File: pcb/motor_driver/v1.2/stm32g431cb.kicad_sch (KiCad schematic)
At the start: 36 parts, among them J3 Conn_ARM_JTAG_SWD_10, J5 Conn, SW1 SKRPACE010, SW2 SKRPACE010, U10 STM32G431CB, U12 MCP2562-E-SN, Y1 XRCGB16M000FXN02R0

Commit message: perf: fix pcb for v1.2
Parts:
- removed SW1, SW2: SKRPACE010, bldc_lib:SKRPACE010, symbol bldc_lib:SKRPACE010
- added SW1: RESET, half_mouse_lib:TVAF06-A020B-R, symbol My_Device:SKRPACE
- added SW2: USER, half_mouse_lib:TVAF06-A020B-R, symbol My_Device:SKRPACE
- C22: renamed from C26; footprint Capacitor_SMD:C_0402_1005Metric -> Capacitor_SMD:C_0603_1608Metric
- C23: renamed from C27; footprint Capacitor_SMD:C_0201_0603Metric -> Capacitor_SMD:C_0603_1608Metric
- C24: renamed from C29; footprint Capacitor_SMD:C_0201_0603Metric -> Capacitor_SMD:C_0603_1608Metric
- C25: renamed from C30; footprint Capacitor_SMD:C_0201_0603Metric -> Capacitor_SMD:C_0603_1608Metric
- C27: renamed from C34; footprint Capacitor_SMD:C_0402_1005Metric -> Capacitor_SMD:C_0603_1608Metric
- C28: renamed from C36; footprint Capacitor_SMD:C_0201_0603Metric -> Capacitor_SMD:C_0603_1608Metric
- D2: renamed from D5; footprint LED_SMD:LED_0402_1005Metric -> LED_SMD:LED_0603_1608Metric
- D3: renamed from D6; footprint LED_SMD:LED_0402_1005Metric -> LED_SMD:LED_0603_1608Metric
- D4: renamed from D7; footprint LED_SMD:LED_0402_1005Metric -> LED_SMD:LED_0603_1608Metric
- D5: renamed from D8; footprint LED_SMD:LED_0402_1005Metric -> LED_SMD:LED_0603_1608Metric
- D6: renamed from D9; footprint LED_SMD:LED_0402_1005Metric -> LED_SMD:LED_0603_1608Metric
- D7: renamed from D10; footprint LED_SMD:LED_0402_1005Metric -> LED_SMD:LED_0603_1608Metric
- R17: renamed from R22; footprint Resistor_SMD:R_0201_0603Metric -> Resistor_SMD:R_0603_1608Metric_Pad0.98x0.95mm_HandSolder
- R18: renamed from R24; footprint Resistor_SMD:R_0201_0603Metric -> Resistor_SMD:R_0603_1608Metric_Pad0.98x0.95mm_HandSolder
- R19: renamed from R23; footprint Resistor_SMD:R_0201_0603Metric -> Resistor_SMD:R_0603_1608Metric_Pad0.98x0.95mm_HandSolder
- R20: renamed from R25; footprint Resistor_SMD:R_0201_0603Metric -> Resistor_SMD:R_0603_1608Metric_Pad0.98x0.95mm_HandSolder
- renumbered C20 to C19, C21 to C20, C25 to C21, C33 to C26, J3 to J4, R14 to R11, R15 to R12, R16 to R13, R17 to R14, R18 to R15, R19 to R16, R26 to R21, R27 to R22, R28 to R23, U10 to U5, U12 to U6
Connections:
- net +3.3V: no longer C26.1
- net GND: now also SW1.2, SW2.1
- net NRST: now also SW1.1
- net SW1: now also C26.1, R18.2, SW2.2
- no-connect marks 3 -> 2
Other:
- moved on the sheet: C21, R18

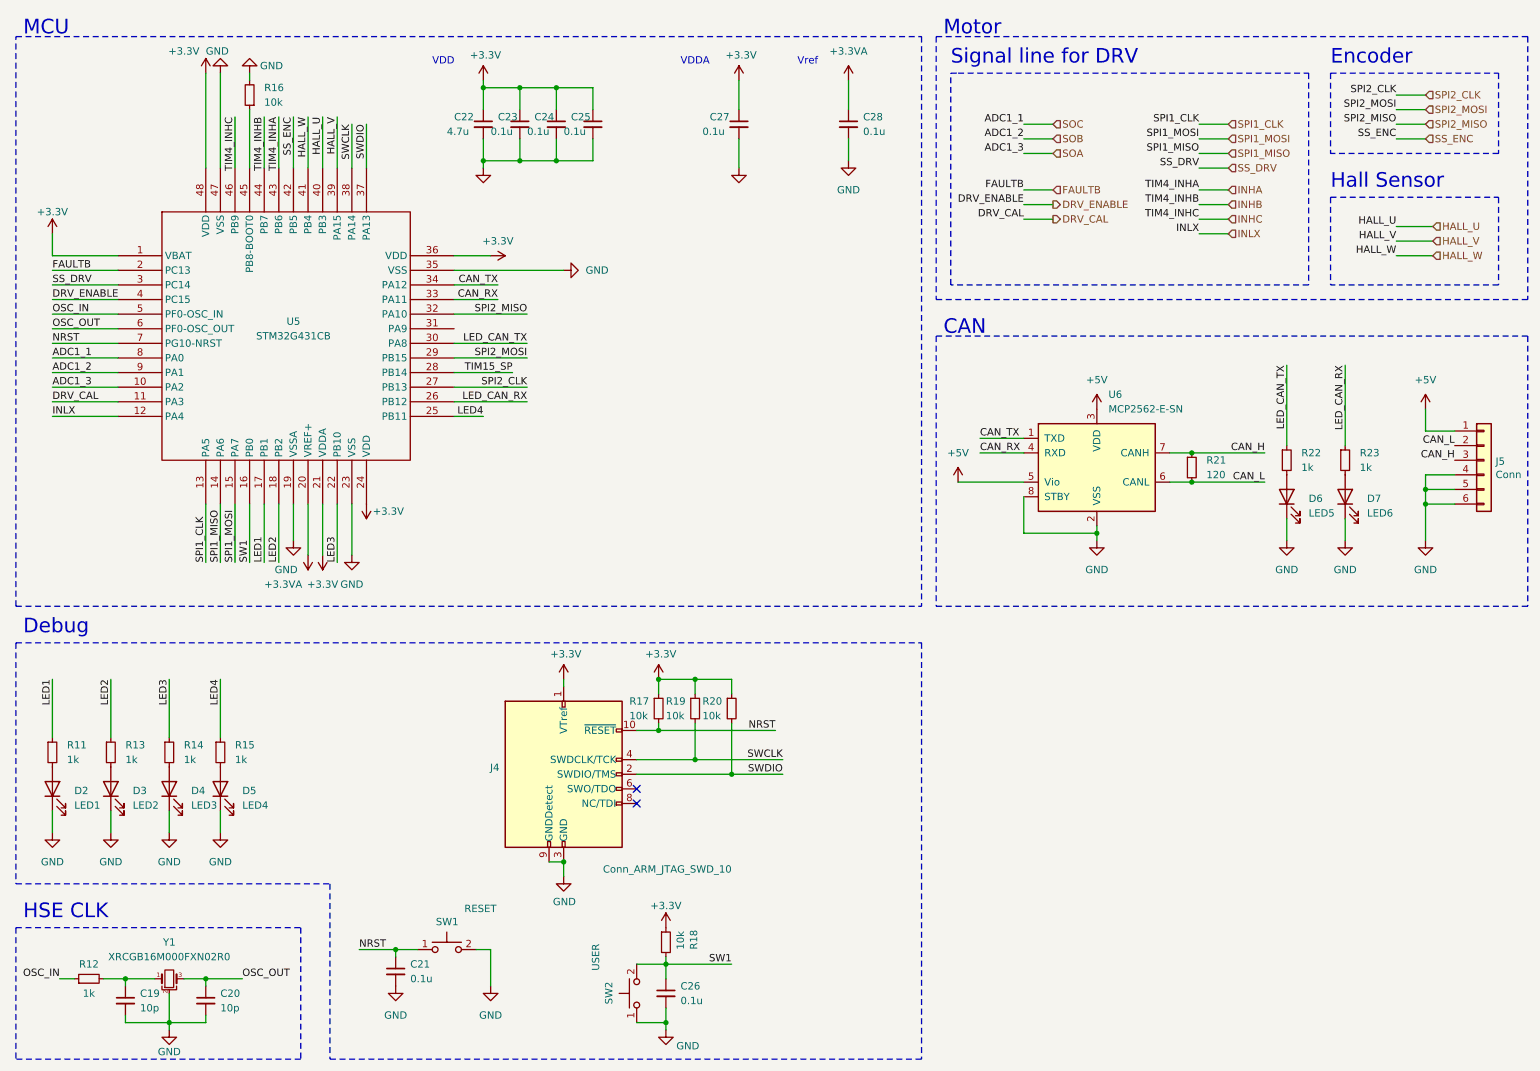
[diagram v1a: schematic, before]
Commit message: perf: update motor driver pdb
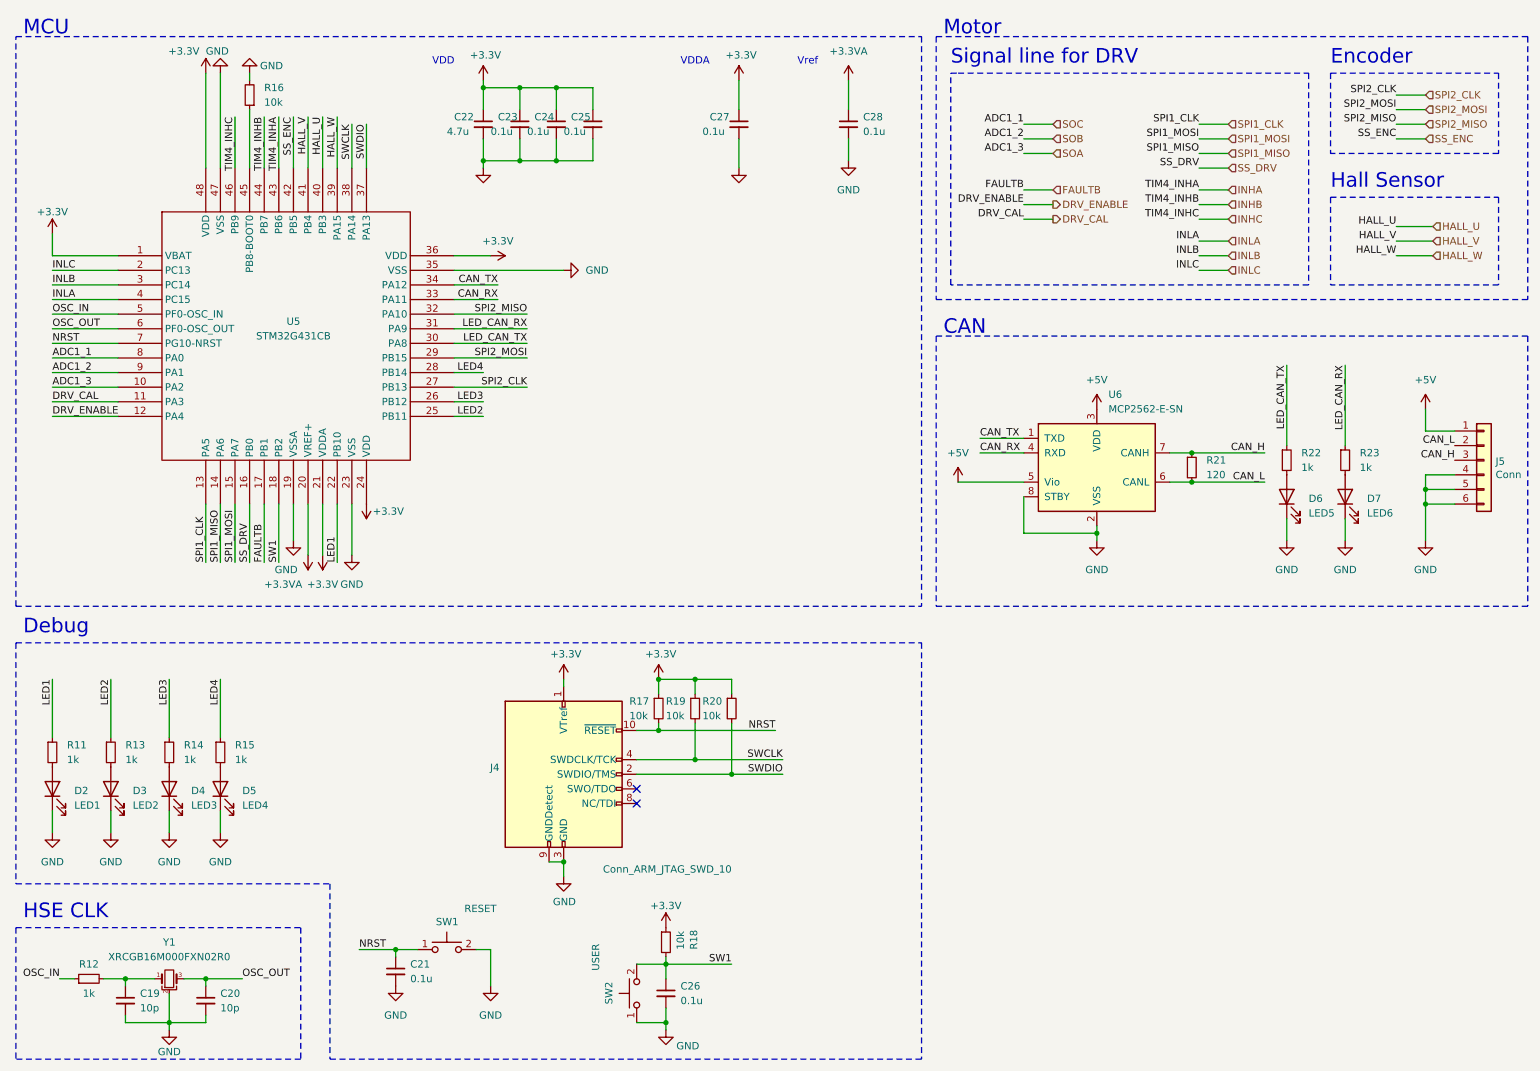
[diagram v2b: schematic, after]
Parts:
- J4: footprint Connector_PinHeader_1.27mm:PinHeader_2x05_P1.27mm_Vertical -> mylib:322110010000
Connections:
- net INLX is gone; now on net DRV_ENABLE: U5.12 (PA4)
- net TIM15_SP is gone; now on net LED4: U5.28 (PB14)
- net DRV_ENABLE: no longer U5.4 (PC15)
- net FAULTB: now also U5.17 (PB1); no longer U5.2 (PC13)
- net HALL_V: now also U5.41 (PB4); no longer U5.39 (PA15)
- net HALL_W: now also U5.39 (PA15); no longer U5.41 (PB4)
- net LED1: now also U5.22 (PB10); no longer U5.17 (PB1)
- net LED2: now also U5.25 (PB11); no longer U5.18 (PB2)
- net LED3: now also U5.26 (PB12); no longer U5.22 (PB10)
- net LED4: no longer U5.25 (PB11)
- net LED_CAN_RX: now also U5.31 (PA9); no longer U5.26 (PB12)
- net SS_DRV: now also U5.16 (PB0); no longer U5.3 (PC14)
- net SW1: now also U5.18 (PB2); no longer U5.16 (PB0)
- new net INLA: U5.4 (PC15)
- new net INLB: U5.3 (PC14)
- new net INLC: U5.2 (PC13)
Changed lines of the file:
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@@
 	(wire
 		(pts
+			(xy 105.41 67.31) (xy 92.71 67.31)
+		)
+		(stroke
+			(width 0)
+			(type default)
+		)
+	)
+	(wire
+		(pts
 			(xy 100.33 62.23) (xy 92.71 62.23)
 		)
@@
 	(wire
 		(pts
-			(xy 92.71 80.01) (xy 105.41 80.01)
+			(xy 92.71 80.01) (xy 97.79 80.01)
 		)
 		(stroke
@@
 	(wire
 		(pts
+			(xy 97.79 74.93) (xy 92.71 74.93)
+		)
+		(stroke
+			(width 0)
+			(type default)
+		)
+	)
+	(wire
+		(pts
 			(xy 220.98 88.9) (xy 217.17 88.9)
 		)
@@
 	(wire
 		(pts
+			(xy 222.25 57.15) (xy 227.33 57.15)
+		)
+		(stroke
+			(width 0)
+			(type default)
+		)
+	)
+	(wire
+		(pts
 			(xy 43.18 187.96) (xy 49.53 187.96)
 		)
@@
 	(wire
 		(pts
-			(xy 102.87 74.93) (xy 92.71 74.93)
-		)
-		(stroke
-			(width 0)
-			(type default)
-		)
-	)
-	(wire
-		(pts
 			(xy 261.62 95.25) (xy 261.62 97.79)
 		)
@@
 	(wire
 		(pts
+			(xy 222.25 54.61) (xy 227.33 54.61)
+		)
+		(stroke
+			(width 0)
+			(type default)
+		)
+	)
+	(wire
+		(pts
 			(xy 184.15 86.36) (xy 191.77 86.36)
 		)
@@
 	(wire
 		(pts
-			(xy 222.25 50.8) (xy 227.33 50.8)
+			(xy 222.25 52.07) (xy 227.33 52.07)
 		)
 		(stroke
@@
 		)
 	)
-	(label "SS_DRV"
+	(label "LED4"
+		(at 97.79 74.93 180)
+		(fields_autoplaced yes)
+		(effects
+			(font
+				(size 1.27 1.27)
+			)
+			(justify right bottom)
+		)
+	)
+	(label "INLB"
 		(at 22.86 59.69 0)
 		(fields_autoplaced yes)
@@
 		)
 	)
-	(label "INLX"
+	(label "DRV_ENABLE"
 		(at 22.86 82.55 0)
 		(fields_autoplaced yes)
@@
 		)
 	)
-	(label "DRV_ENABLE"
+	(label "INLA"
 		(at 22.86 62.23 0)
 		(fields_autoplaced yes)
@@
 		)
 	)
-	(label "LED4"
+	(label "LED_CAN_RX"
+		(at 105.41 67.31 180)
+		(fields_autoplaced yes)
+		(effects
+			(font
+				(size 1.27 1.27)
+			)
+			(justify right bottom)
+		)
+	)
+	(label "LED2"
 		(at 97.79 82.55 180)
 		(fields_autoplaced yes)
@@
 		)
 	)
+	(label "INLC"
+		(at 222.25 57.15 180)
+		(fields_autoplaced yes)
+		(effects
+			(font
+				(size 1.27 1.27)
+			)
+			(justify right bottom)
+		)
+	)
 	(label "ADC1_2"
 		(at 191.77 34.29 180)
@@
 		)
 	)
-	(label "LED_CAN_RX"
-		(at 105.41 80.01 180)
+	(label "LED3"
+		(at 97.79 80.01 180)
 		(fields_autoplaced yes)
 		(effects
@@
 		)
 	)
-	(label "LED1"
+	(label "FAULTB"
 		(at 59.69 107.95 90)
 		(fields_autoplaced yes)
@@
 		)
 	)
-	(label "TIM15_SP"
-		(at 102.87 74.93 180)
-		(fields_autoplaced yes)
-		(effects
-			(font
-				(size 1.27 1.27)
-			)
-			(justify right bottom)
-		)
-	)
 	(label "DRV_ENABLE"
 		(at 191.77 45.72 180)
@@
 		)
 	)
-	(label "SW1"
+	(label "SS_DRV"
 		(at 57.15 107.95 90)
 		(fields_autoplaced yes)
@@
 		)
 	)
+	(label "INLB"
+		(at 222.25 54.61 180)
+		(fields_autoplaced yes)
+		(effects
+			(font
+				(size 1.27 1.27)
+			)
+			(justify right bottom)
+		)
+	)
 	(label "OSC_IN"
 		(at 24.13 180.34 180)
@@
 		)
 	)
-	(label "INLX"
-		(at 222.25 50.8 180)
+	(label "INLA"
+		(at 222.25 52.07 180)
 		(fields_autoplaced yes)
 		(effects
@@
 		)
 	)
-	(label "LED2"
+	(label "SW1"
 		(at 62.23 107.95 90)
 		(fields_autoplaced yes)
@@
 		)
 	)
-	(label "FAULTB"
+	(label "INLC"
 		(at 22.86 57.15 0)
 		(fields_autoplaced yes)
@@
 		)
 	)
-	(label "HALL_V"
+	(label "HALL_W"
 		(at 72.39 30.48 270)
 		(fields_autoplaced yes)
@@
 		)
 	)
-	(label "LED3"
+	(label "LED1"
 		(at 72.39 107.95 90)
 		(fields_autoplaced yes)
@@
 		)
 	)
-	(label "HALL_W"
+	(label "HALL_V"
 		(at 67.31 30.48 270)
 		(fields_autoplaced yes)
@@
 		)
 	)
-	(hierarchical_label "INLX"
+	(hierarchical_label "INLA"
 		(shape input)
-		(at 227.33 50.8 0)
+		(at 227.33 52.07 0)
 		(fields_autoplaced yes)
 		(effects
@@
 		)
 	)
+	(hierarchical_label "INLB"
+		(shape input)
+		(at 227.33 54.61 0)
+		(fields_autoplaced yes)
+		(effects
+			(font
+				(size 1.27 1.27)
+			)
+			(justify left)
+		)
+	)
+	(hierarchical_label "INLC"
+		(shape input)
+		(at 227.33 57.15 0)
+		(fields_autoplaced yes)
+		(effects
+			(font
+				(size 1.27 1.27)
+			)
+			(justify left)
+		)
+	)
 	(hierarchical_label "INHA"
 		(shape input)
@@
 			)
 		)
-		(property "Footprint" "Connector_PinHeader_1.27mm:PinHeader_2x05_P1.27mm_Vertical"
+		(property "Footprint" "mylib:322110010000"
 			(at 113.03 158.75 0)
 			(effects

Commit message: feat: add additional CAN connetctor
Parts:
- added J5: Conn, mylib:21322604YY, symbol Connector_Generic:Conn_01x06
- J4: renamed from J5; footprint bldc_lib:21322604YY -> mylib:21322604YY
- renumbered D2 to D3, D3 to D4, D4 to D5, D5 to D6, D6 to D7, D7 to D8, J4 to J3, R11 to R12, R12 to R13, R13 to R14, R14 to R15, R15 to R16, R16 to R17, R17 to R18, R18 to R19, R19 to R20, R20 to R21, R21 to R22, R22 to R23, R23 to R24
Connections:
- net +5V: now also J5.1 (Pin_1)
- net CAN_H: now also J5.3 (Pin_3)
- net CAN_L: now also J5.2 (Pin_2)
- net GND: now also R23.2, R24.2, J5.4 (Pin_4), J5.5 (Pin_5), J5.6 (Pin_6); no longer D7.1 (K), D8.1 (K)
- net LED_CAN_RX: now also D8.2 (A); no longer R24.1
- net LED_CAN_TX: now also D7.2 (A); no longer R23.1
- new net: D8.1 (K), R24.1
- new net: D7.1 (K), R23.1
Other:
- moved on the sheet: D7, D8, J4, R23, R24
